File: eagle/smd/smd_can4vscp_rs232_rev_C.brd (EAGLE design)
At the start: 71.9 x 42.4 mm, 31 parts, among them IC1 PIC18F2580, IC3 MCP2551SN, IC4 LM2575S, IC7 ST232B (0.1uF)/MAX232IDWR (1u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, J2 A00-108-220-450, Q1 HC-49S

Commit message: Added switches for RS-232/TTL
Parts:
- added J5, J6: (no value), con-lstb:MA03-1
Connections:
- new net RXIF: IC7.12, J5.3
- new net RXTTL: J3.2, J5.1
- new net TXIF: IC7.11, J6.3
- new net TXTTL: J3.3, J6.1
- net RX: now also J5.2; no longer IC7.12, J3.2
- net TX: now also J6.2; no longer IC7.11, J3.3
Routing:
- net RXIF: track 0.00 -> 35.9 mm, vias 0 -> 1
- net TXIF: track 0.00 -> 29.7 mm, vias 0 -> 1
- net TX: track 64.4 -> 48.2 mm, vias 0 -> 1
- net TXTTL: track 0.00 -> 11.1 mm
- net RXTTL: track 0.00 -> 4.80 mm
- net RX: track 63.6 -> 61.4 mm, vias 1 -> 2
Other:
- board text added: "GND"
- board text added: "POW"
- board text added: "RS232"
- board text added: "RX"
- board text added: "TTL"
- board text added: "TX"

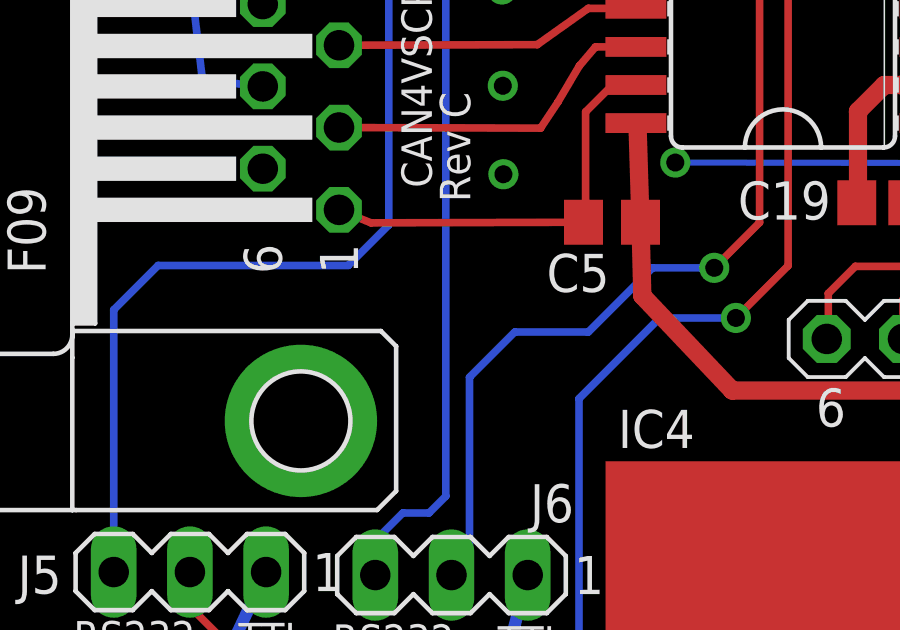
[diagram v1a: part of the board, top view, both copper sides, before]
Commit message: All verbose commands now return +OK
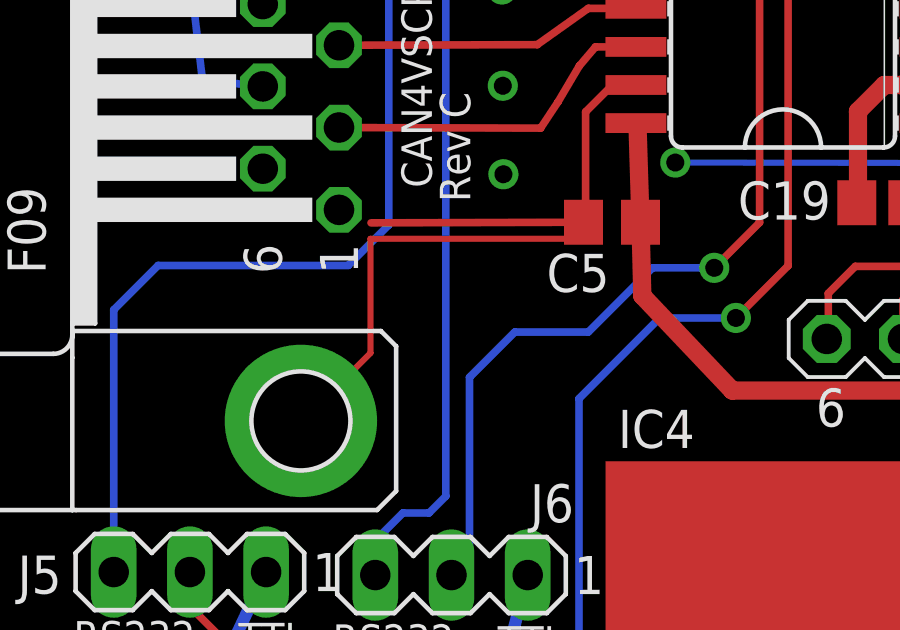
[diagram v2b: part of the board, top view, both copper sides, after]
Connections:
- net GND: now also J4.5; no longer J4.1
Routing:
- net GND: track 69.3 -> 83.6 mm
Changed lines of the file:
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@@
 <contactref element="IC3" pad="8"/>
 <contactref element="D2" pad="3"/>
-<contactref element="J4" pad="1"/>
 <contactref element="J4" pad="G1"/>
 <contactref element="IC7" pad="15"/>
@@
 <wire x1="22.34" y1="19.6" x2="22.41" y2="19.63" width="0.254" layer="1"/>
 <wire x1="15.2564" y1="19.58" x2="22.34" y2="19.6" width="0.254" layer="1"/>
-<wire x1="14.19" y1="20.0136" x2="15.2564" y2="19.58" width="0.254" layer="1"/>
 <wire x1="33.15" y1="20.25" x2="34.5" y2="20.25" width="0.6096" layer="1"/>
 <wire x1="34.5" y1="20.25" x2="34.56" y2="20.31" width="0.254" layer="1"/>
@@
 <via x="19.65" y="24.15" extent="1-16" drill="0.6" shape="square"/>
 <via x="19.67" y="21.2" extent="1-16" drill="0.6" shape="square"/>
+<contactref element="J4" pad="5"/>
+<wire x1="15.24" y1="19.05" x2="22.86" y2="19.05" width="0.2032" layer="1"/>
+<wire x1="15.24" y1="15.24" x2="15.24" y2="19.05" width="0.2032" layer="1"/>
+<wire x1="13.97" y1="13.97" x2="15.24" y2="15.24" width="0.2032" layer="1"/>
+<wire x1="22.86" y1="19.05" x2="22.34" y2="19.6" width="0.2032" layer="1"/>
+<wire x1="13.97" y1="13.97" x2="12.92" y2="12.9778" width="0.2032" layer="1"/>
 </signal>
 <signal name="VCC">

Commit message: First release
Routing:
- net GND: track 83.6 -> 76.5 mm, vias 14 -> 15
- net RTS_IN: track 39.6 -> 39.0 mm
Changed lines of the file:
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@@
 <wire x1="22.41" y1="19.63" x2="22.41" y2="23.28" width="0.254" layer="1"/>
 <wire x1="22.34" y1="19.6" x2="22.41" y2="19.63" width="0.254" layer="1"/>
-<wire x1="15.2564" y1="19.58" x2="22.34" y2="19.6" width="0.254" layer="1"/>
 <wire x1="33.15" y1="20.25" x2="34.5" y2="20.25" width="0.6096" layer="1"/>
 <wire x1="34.5" y1="20.25" x2="34.56" y2="20.31" width="0.254" layer="1"/>
@@
 <wire x1="22.86" y1="19.05" x2="22.34" y2="19.6" width="0.2032" layer="1"/>
 <wire x1="13.97" y1="13.97" x2="12.92" y2="12.9778" width="0.2032" layer="1"/>
+<via x="15.73" y="30.93" extent="1-16" drill="0.6" shape="square"/>
+<wire x1="65.82" y1="32.51" x2="69.6586" y2="33.2514" width="0" layer="19" extent="1-1"/>
+<wire x1="55.88" y1="33.02" x2="64.47" y2="32.52" width="0" layer="19" extent="1-1"/>
+<wire x1="50.95" y1="32.525" x2="54.61" y2="34.29" width="0" layer="19" extent="1-1"/>
+<wire x1="38.1" y1="31.75" x2="40.79" y2="35.065" width="0" layer="19" extent="1-1"/>
+<wire x1="55.26" y1="27.28" x2="55.88" y2="31.75" width="0" layer="19" extent="1-1"/>
+<wire x1="55.26" y1="24.7" x2="55.26" y2="27.28" width="0" layer="19" extent="1-1"/>
+<wire x1="57.84" y1="26" x2="55.26" y2="27.28" width="0" layer="19" extent="1-1"/>
+<wire x1="48.085" y1="17.39" x2="55.26" y2="24.7" width="0" layer="19" extent="1-1"/>
+<wire x1="44.45" y1="8.89" x2="49.355" y2="12.19" width="0" layer="19" extent="1-1"/>
+<wire x1="36.6106" y1="9.6376" x2="36.6106" y2="6.234" width="0" layer="19" extent="1-1"/>
+<wire x1="38.07" y1="15.71" x2="37.05" y2="11.78" width="0" layer="19" extent="1-1"/>
+<wire x1="34.5" y1="20.25" x2="38.07" y2="15.71" width="0" layer="19" extent="1-1"/>
+<wire x1="56.38" y1="13.84" x2="50.25" y2="12.19" width="0" layer="19" extent="1-1"/>
+<wire x1="24.0878" y1="24.175" x2="33.15" y2="20.25" width="0" layer="19" extent="1-1"/>
+<wire x1="19.65" y1="24.15" x2="22.41" y2="23.28" width="0" layer="19" extent="1-1"/>
+<wire x1="19.67" y1="21.2" x2="19.65" y2="24.15" width="0" layer="19" extent="1-1"/>
+<wire x1="19.62" y1="27.36" x2="19.65" y2="24.15" width="0" layer="19" extent="1-1"/>
+<wire x1="15.73" y1="30.93" x2="19.62" y2="27.36" width="0" layer="19" extent="1-1"/>
+<wire x1="14.19" y1="30.9864" x2="15.73" y2="30.93" width="0" layer="19" extent="1-1"/>
+<wire x1="14.79" y1="3.6" x2="12.92" y2="12.9778" width="0" layer="19" extent="1-1"/>
+<wire x1="69.6276" y1="11.2958" x2="57.8475" y2="13.84" width="0" layer="19" extent="1-1"/>
 </signal>
 <signal name="VCC">
@@
 <wire x1="14.44" y1="34.29" x2="31.56" y2="34.29" width="0.254" layer="16"/>
 <wire x1="12.18" y1="34.32" x2="14.44" y2="34.29" width="0.254" layer="16"/>
-<wire x1="9.26" y1="27.53" x2="9.22" y2="33.49" width="0.254" layer="16"/>
-<wire x1="9.22" y1="33.49" x2="9.85" y2="34.11" width="0.254" layer="16"/>
-<wire x1="9.85" y1="34.11" x2="12.18" y2="34.32" width="0.254" layer="16"/>
-<wire x1="9.63" y1="24.41" x2="9.26" y2="27.53" width="0.254" layer="16"/>
-<wire x1="9.63" y1="24.41" x2="12.2116" y2="23.99" width="0.254" layer="16"/>
+<wire x1="9.5" y1="25.67" x2="9.47" y2="33.59" width="0.254" layer="16"/>
+<wire x1="9.47" y1="33.59" x2="10.73" y2="34.29" width="0.254" layer="16"/>
+<wire x1="10.73" y1="34.29" x2="12.18" y2="34.32" width="0.254" layer="16"/>
+<wire x1="9.9" y1="24.59" x2="9.5" y2="25.67" width="0.254" layer="16"/>
+<wire x1="9.9" y1="24.59" x2="12.2116" y2="23.99" width="0.254" layer="16"/>
 <wire x1="12.2116" y1="23.99" x2="11.65" y2="24.1284" width="0.254" layer="16"/>
 <via x="31.56" y="34.29" extent="1-16" drill="0.6" shape="square"/>

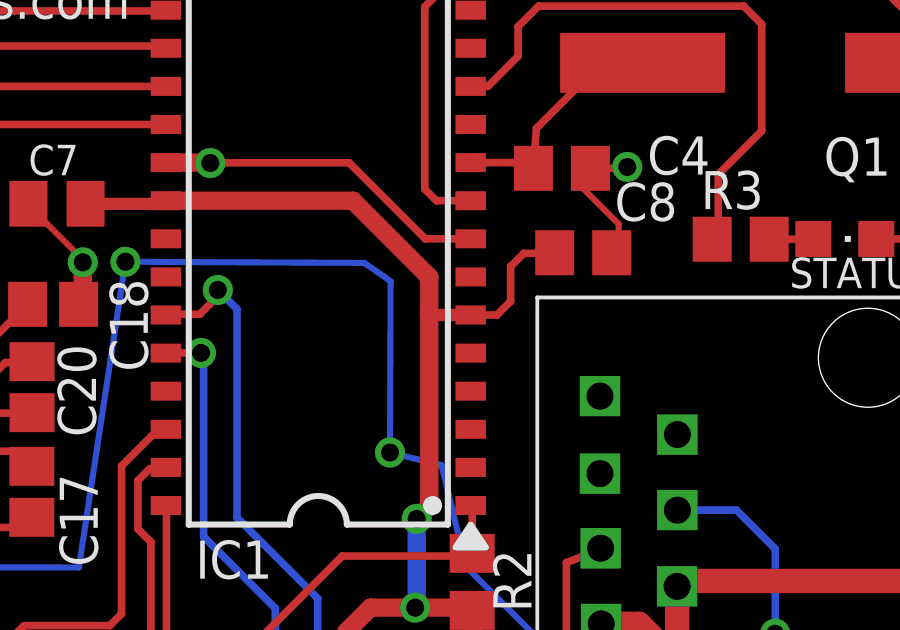
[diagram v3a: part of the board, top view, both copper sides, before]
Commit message: Removed VCC from VCAP.
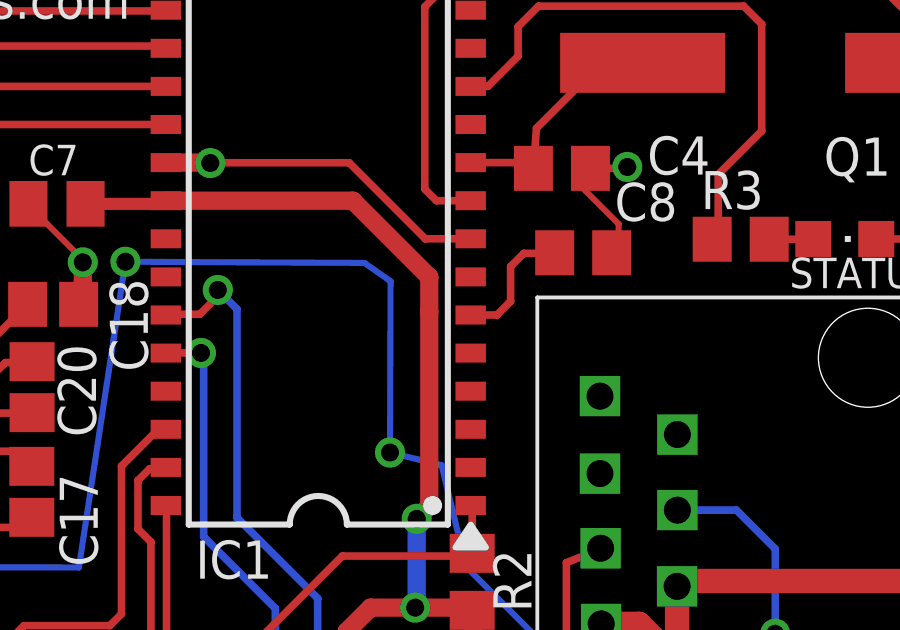
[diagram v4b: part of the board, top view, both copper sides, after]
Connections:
- new net N$8: C8.2, IC1.6
- net VCC: no longer C8.2, IC1.6
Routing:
- net VCC: track 115.2 -> 109.5 mm
- net N$8: track 0.00 -> 4.34 mm
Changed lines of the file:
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@@
 <via x="49.15" y="23.19" extent="1-16" drill="0.6" shape="square"/>
 <via x="49.1" y="20.23" extent="1-16" drill="0.6" shape="square"/>
-<contactref element="C8" pad="2"/>
-<contactref element="IC1" pad="6"/>
-<wire x1="50.95" y1="29.985" x2="51.825" y2="29.985" width="0.254" layer="1"/>
-<wire x1="51.825" y1="29.985" x2="52.28" y2="30.44" width="0.254" layer="1"/>
-<wire x1="52.28" y1="30.44" x2="52.28" y2="31.6" width="0.254" layer="1"/>
-<wire x1="52.28" y1="31.6" x2="52.72" y2="32.04" width="0.254" layer="1"/>
-<wire x1="52.72" y1="32.04" x2="53.73" y2="32.04" width="0.254" layer="1"/>
-<wire x1="53.73" y1="32.04" x2="53.75" y2="32.06" width="0.254" layer="1"/>
-<wire x1="50.95" y1="29.985" x2="49.57" y2="29.985" width="0.4064" layer="1"/>
 <wire x1="49.57" y1="29.985" x2="49.57" y2="30.09" width="0.4064" layer="1"/>
 <contactref element="C7" pad="2"/>
@@
 <wire x1="9.71" y1="3.6" x2="11.76" y2="7.94" width="0.4064" layer="16"/>
 </signal>
+<signal name="N$8">
+<contactref element="C8" pad="2"/>
+<contactref element="IC1" pad="6"/>
+<wire x1="50.95" y1="29.985" x2="51.825" y2="29.985" width="0.254" layer="1"/>
+<wire x1="51.825" y1="29.985" x2="52.28" y2="30.44" width="0.254" layer="1"/>
+<wire x1="52.28" y1="30.44" x2="52.28" y2="31.6" width="0.254" layer="1"/>
+<wire x1="52.28" y1="31.6" x2="52.72" y2="32.04" width="0.254" layer="1"/>
+<wire x1="52.72" y1="32.04" x2="53.73" y2="32.04" width="0.254" layer="1"/>
+<wire x1="53.73" y1="32.04" x2="53.75" y2="32.06" width="0.254" layer="1"/>
+</signal>
 </signals>

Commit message: RA4 set to input to prevent collision with VCAP circuits in PIC18F2580. Brown out raised to maximum (3V & 4.6V). Valuable input from Anders Forsgren, AJE Electronics AB.
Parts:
- C8: value 1 uF -> 10 uF
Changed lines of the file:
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@@
 <attribute name="OC_NEWARK" value="unknown" x="10.98" y="3.6" size="1.016" layer="27" font="fixed" display="off"/>
 </element>
-<element name="C8" library="rcl" package="C0805" value="1 uF" x="54.7" y="32.06" smashed="yes" rot="R180">
+<element name="C8" library="rcl" package="C0805" value="10 uF" x="54.7" y="32.06" smashed="yes" rot="R180">
 <attribute name="NAME" x="57.84" y="34.39" size="1.27" layer="25" font="fixed" rot="R180"/>
 </element>
